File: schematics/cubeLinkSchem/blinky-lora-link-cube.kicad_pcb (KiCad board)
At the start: 2 copper layers, 67 x 34.5 mm, 5 parts, among them J1 SMA Ant, U1 RPIHeader, U2 FEATHER_M0_BASIC_PROTO

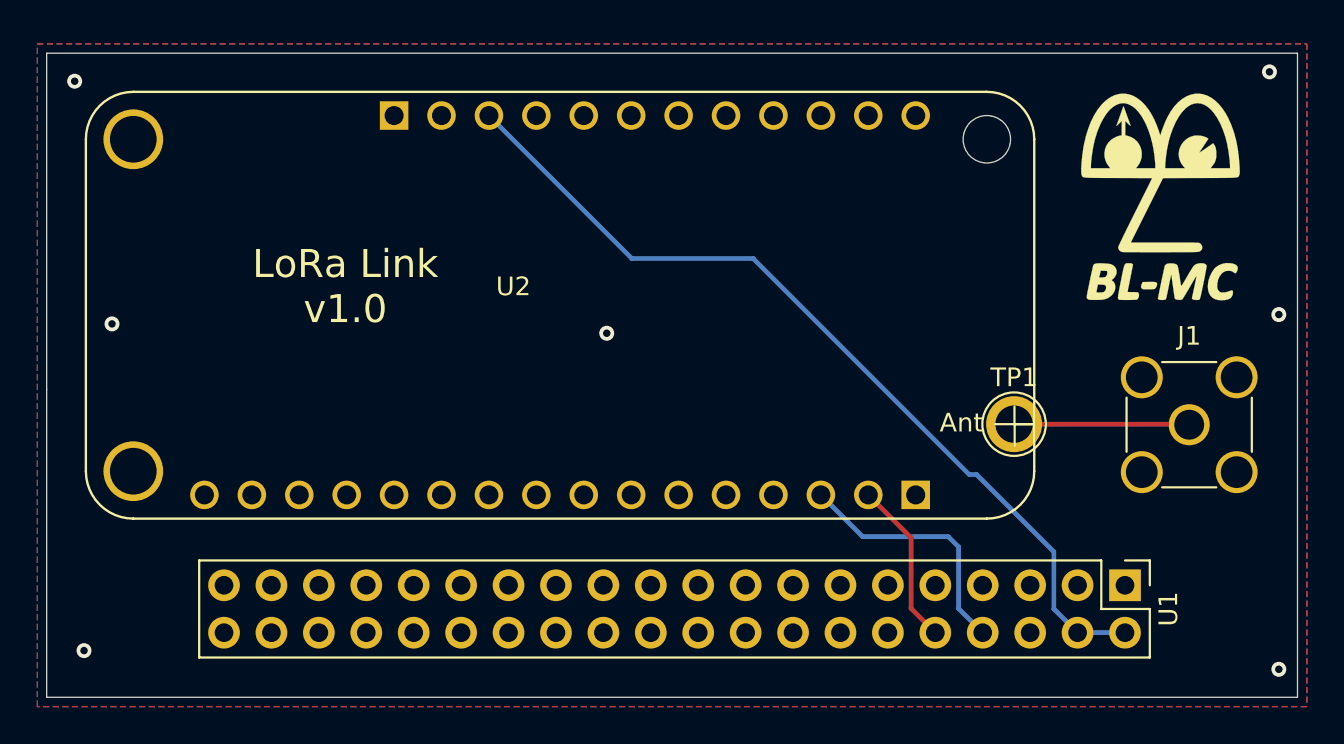
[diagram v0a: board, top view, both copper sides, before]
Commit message: fixed lora footprint
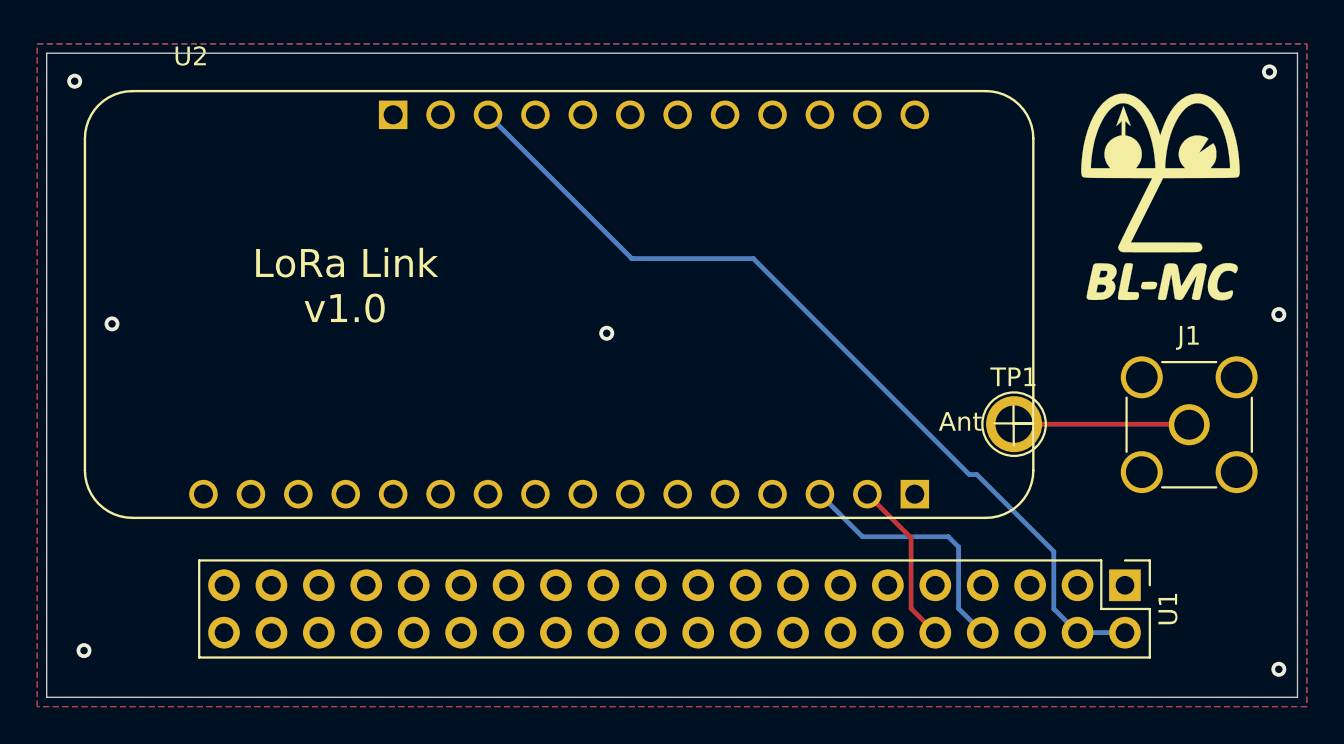
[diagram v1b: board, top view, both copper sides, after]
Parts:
- U2: value FEATHER_M0_BASIC_PROTO -> FeatherM0LoRa; footprint FEATHER_M0_BASIC_PROTO:MODULE_FEATHER_M0_BASIC_PROTO -> dmcginnis427Footprints:FeatherM0LoRa
- moved U2 0.06 mm to (118.0, 81.0)
